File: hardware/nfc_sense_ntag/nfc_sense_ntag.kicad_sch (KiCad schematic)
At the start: 16 parts, among them U1 TMP117AIDRVR

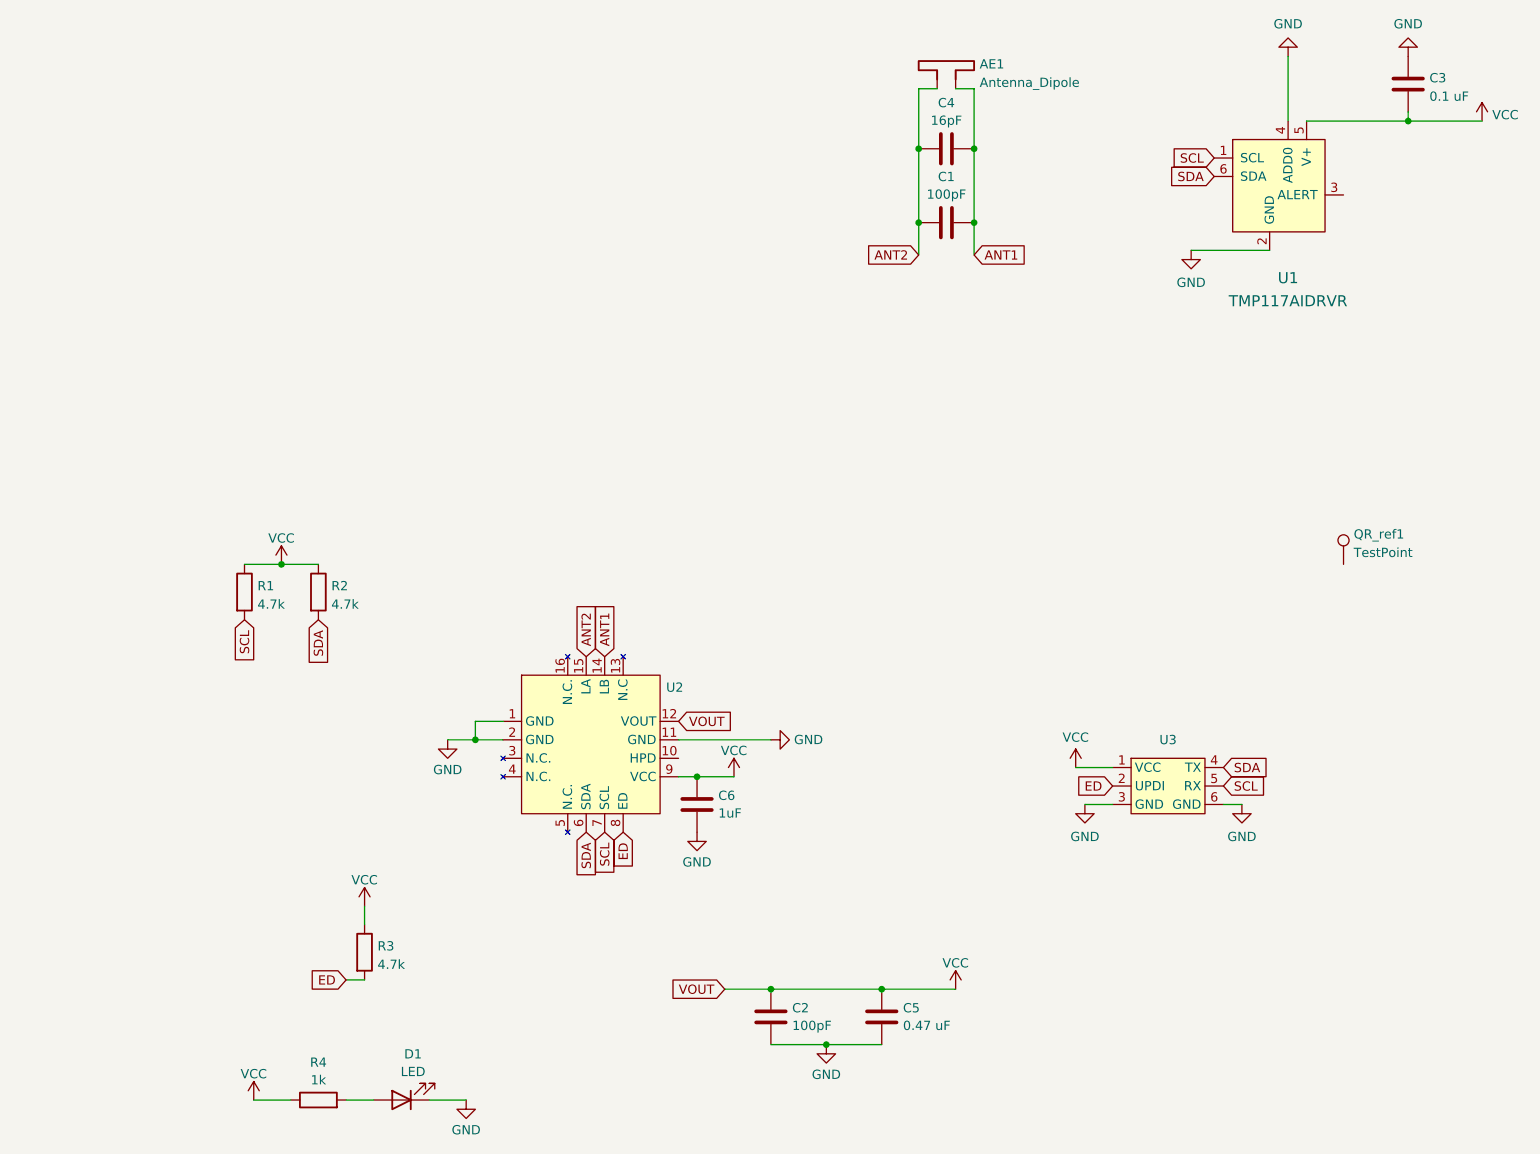
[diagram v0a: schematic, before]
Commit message: update nfc sense ntag with attiny 1626
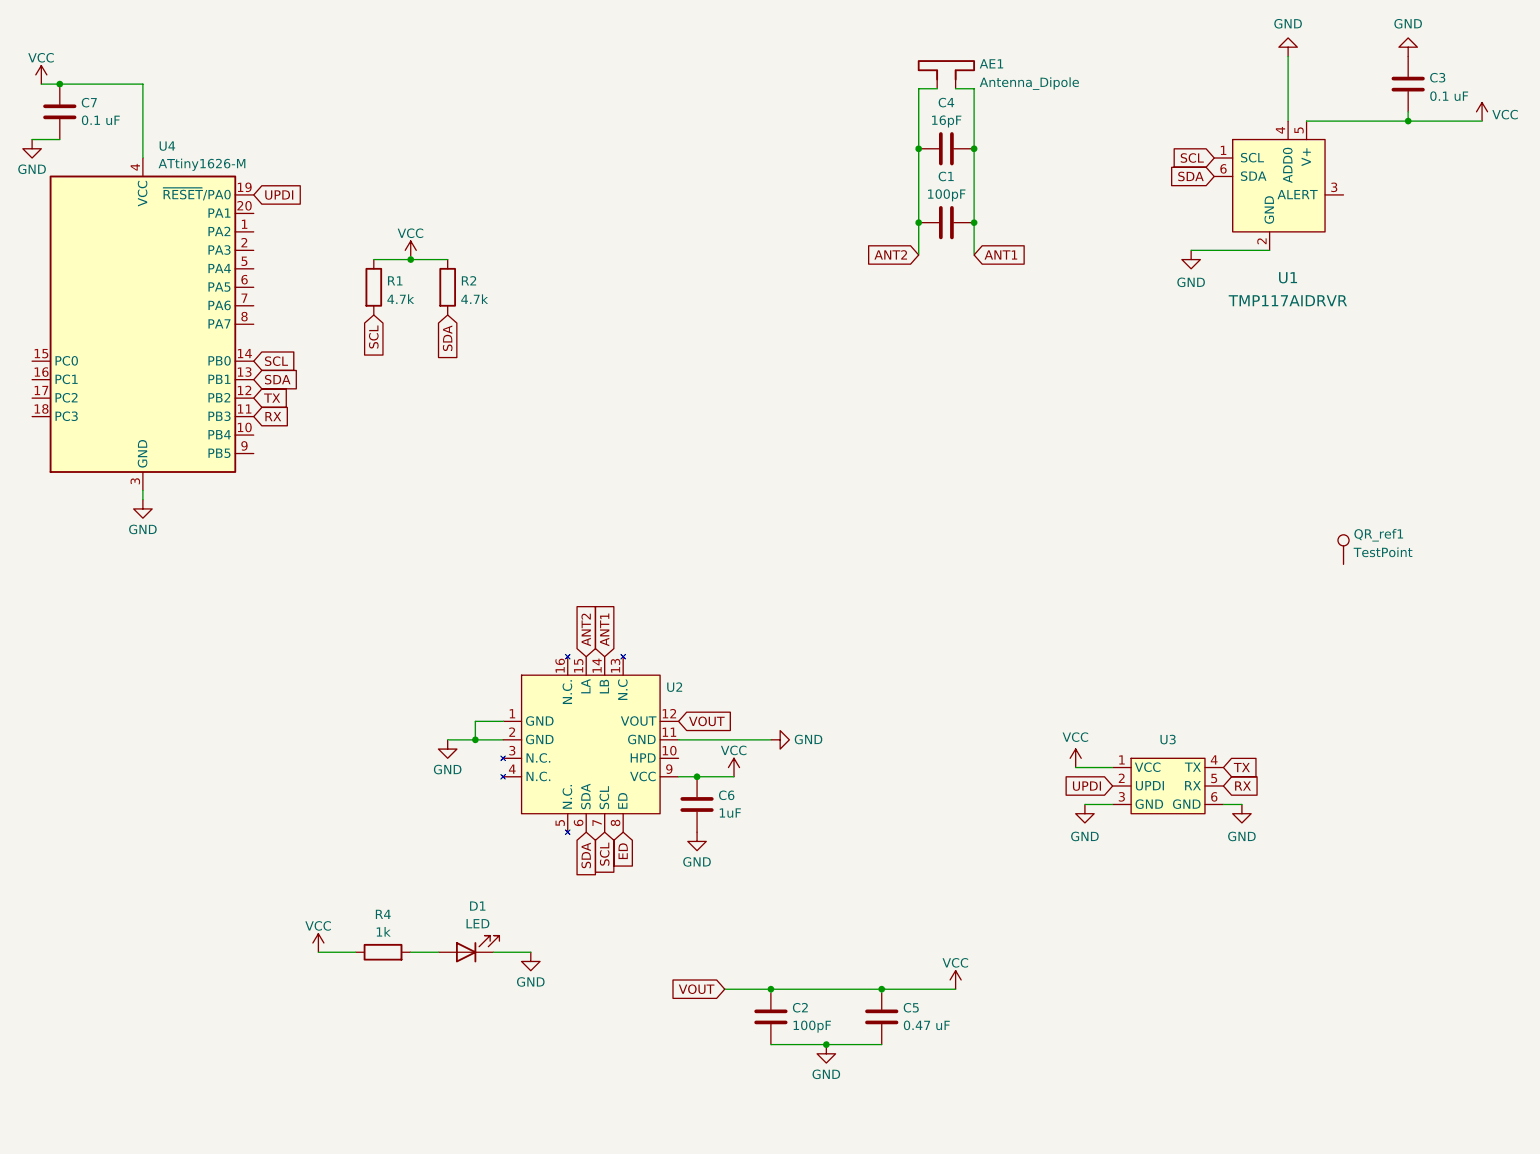
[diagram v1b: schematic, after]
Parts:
- removed R3: 4.7k, Resistor_SMD:R_0603_1608Metric, symbol Device:R
- added C7: 0.1 uF, Capacitor_SMD:C_0603_1608Metric, symbol Device:C
- added U4: ATtiny1626-M, Package_DFN_QFN:VQFN-20-1EP_3x3mm_P0.4mm_EP1.7x1.7mm, symbol MCU_Microchip_ATtiny:ATtiny1626-M
- U2, U3: value ~ -> (none)
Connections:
- net ED: no longer U3.2 (UPDI)
- net GND: now also C7.2, U4.21 (GND), U4.3 (GND)
- net SCL: now also U4.14 (PB0); no longer U3.5 (RX)
- net SDA: now also U4.13 (PB1); no longer U3.4 (TX)
- net VCC: now also C7.1, U4.4 (VCC)
- new net RX: U3.5 (RX), U4.11 (PB3)
- new net TX: U3.4 (TX), U4.12 (PB2)
- new net UPDI: U3.2 (UPDI), U4.19 (~{RESET}/PA0)
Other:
- moved on the sheet: D1, R1, R2, R4
